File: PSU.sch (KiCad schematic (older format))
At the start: 11 parts

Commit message: Component placement
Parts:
- added J9: Conn_01x02, Connector_PinHeader_2.54mm:PinHeader_1x02_P2.54mm_Vertical, symbol Connector_Generic:Conn_01x02
- C1, C2: renamed from C?; footprint (none) -> Capacitor_SMD:C_0402_1005Metric
- D1, D2: renamed from D?; footprint (none) -> LED_SMD:LED_0603_1608Metric
- R3, R4, R5: renamed from R?; footprint (none) -> Resistor_SMD:R_0402_1005Metric
- gave numbers to parts that had none: 4
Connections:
- net GND: now also J9.2 (Pin_2)
- net VEXT: now also J9.1 (Pin_1)
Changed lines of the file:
@@
 $Descr A4 11693 8268
 encoding utf-8
-Sheet 2 5
+Sheet 2 4
 Title ""
 Date ""
@@
 P 7400 2200
 AR Path="/61CE9B73" Ref="U?"  Part="1"
-AR Path="/61CDC1C0/61CE9B73" Ref="U?"  Part="1"
-F 0 "U?" H 7400 2442 50  0000 C CNN
+AR Path="/61CDC1C0/61CE9B73" Ref="U1"  Part="1"
+F 0 "U1" H 7400 2442 50  0000 C CNN
 F 1 "AMS1117-3.3" H 7400 2351 50  0000 C CNN
 F 2 "Package_TO_SOT_SMD:SOT-223-3_TabPin2" H 7400 2400 50  0001 C CNN
@@
 P 7900 2400
 AR Path="/61CE9B79" Ref="C?"  Part="1"
-AR Path="/61CDC1C0/61CE9B79" Ref="C?"  Part="1"
-F 0 "C?" H 7988 2446 50  0000 L CNN
+AR Path="/61CDC1C0/61CE9B79" Ref="C2"  Part="1"
+F 0 "C2" H 7988 2446 50  0000 L CNN
 F 1 "22uF" H 7988 2355 50  0000 L CNN
-F 2 "" H 7900 2400 50  0001 C CNN
+F 2 "Capacitor_SMD:C_0402_1005Metric" H 7900 2400 50  0001 C CNN
 F 3 "~" H 7900 2400 50  0001 C CNN
 	1    7900 2400
@@
 P 6850 2400
 AR Path="/61CE9B7F" Ref="C?"  Part="1"
-AR Path="/61CDC1C0/61CE9B7F" Ref="C?"  Part="1"
-F 0 "C?" H 6938 2446 50  0000 L CNN
+AR Path="/61CDC1C0/61CE9B7F" Ref="C1"  Part="1"
+F 0 "C1" H 6938 2446 50  0000 L CNN
 F 1 "47uF" H 6938 2355 50  0000 L CNN
-F 2 "" H 6850 2400 50  0001 C CNN
+F 2 "Capacitor_SMD:C_0402_1005Metric" H 6850 2400 50  0001 C CNN
 F 3 "~" H 6850 2400 50  0001 C CNN
 	1    6850 2400
@@
 P 6850 2650
 AR Path="/61CE9B8F" Ref="#PWR?"  Part="1"
-AR Path="/61CDC1C0/61CE9B8F" Ref="#PWR?"  Part="1"
-F 0 "#PWR?" H 6850 2400 50  0001 C CNN
+AR Path="/61CDC1C0/61CE9B8F" Ref="#PWR022"  Part="1"
+F 0 "#PWR022" H 6850 2400 50  0001 C CNN
 F 1 "GND" H 6855 2477 50  0001 C CNN
 F 2 "" H 6850 2650 50  0001 C CNN
@@
 P 7900 2150
 AR Path="/61CE9B97" Ref="#PWR?"  Part="1"
-AR Path="/61CDC1C0/61CE9B97" Ref="#PWR?"  Part="1"
-F 0 "#PWR?" H 7900 2000 50  0001 C CNN
+AR Path="/61CDC1C0/61CE9B97" Ref="#PWR023"  Part="1"
+F 0 "#PWR023" H 7900 2000 50  0001 C CNN
 F 1 "+3V3" H 7915 2323 50  0000 C CNN
 F 2 "" H 7900 2150 50  0001 C CNN
@@
 P 6850 2150
 AR Path="/61CE9B9F" Ref="#PWR?"  Part="1"
-AR Path="/61CDC1C0/61CE9B9F" Ref="#PWR?"  Part="1"
-F 0 "#PWR?" H 6850 2000 50  0001 C CNN
+AR Path="/61CDC1C0/61CE9B9F" Ref="#PWR021"  Part="1"
+F 0 "#PWR021" H 6850 2000 50  0001 C CNN
 F 1 "+5V" H 6865 2323 50  0000 C CNN
 F 2 "" H 6850 2150 50  0001 C CNN
@@
 P 5000 3200
 AR Path="/61CE9BC3" Ref="#PWR?"  Part="1"
-AR Path="/61CDC1C0/61CE9BC3" Ref="#PWR?"  Part="1"
-F 0 "#PWR?" H 5000 2950 50  0001 C CNN
+AR Path="/61CDC1C0/61CE9BC3" Ref="#PWR019"  Part="1"
+F 0 "#PWR019" H 5000 2950 50  0001 C CNN
 F 1 "GND" H 5005 3027 50  0001 C CNN
 F 2 "" H 5000 3200 50  0001 C CNN
@@
 P 5000 2400
 AR Path="/61CE9BCE" Ref="R?"  Part="1"
-AR Path="/61CDC1C0/61CE9BCE" Ref="R?"  Part="1"
-F 0 "R?" H 5059 2446 50  0000 L CNN
+AR Path="/61CDC1C0/61CE9BCE" Ref="R4"  Part="1"
+F 0 "R4" H 5059 2446 50  0000 L CNN
 F 1 "47k" H 5059 2355 50  0000 L CNN
-F 2 "" H 5000 2400 50  0001 C CNN
+F 2 "Resistor_SMD:R_0402_1005Metric" H 5000 2400 50  0001 C CNN
 F 3 "~" H 5000 2400 50  0001 C CNN
 	1    5000 2400
@@
 P 4900 2950
 AR Path="/61CE9BD4" Ref="Q?"  Part="1"
-AR Path="/61CDC1C0/61CE9BD4" Ref="Q?"  Part="1"
-F 0 "Q?" H 5105 2996 50  0000 L CNN
+AR Path="/61CDC1C0/61CE9BD4" Ref="Q2"  Part="1"
+F 0 "Q2" H 5105 2996 50  0000 L CNN
 F 1 "AO3400A" H 5105 2905 50  0000 L CNN
 F 2 "Package_TO_SOT_SMD:SOT-23" H 5100 2875 50  0001 L CIN
@@
 P 4650 2300
 AR Path="/61CE9BDB" Ref="Q?"  Part="1"
-AR Path="/61CDC1C0/61CE9BDB" Ref="Q?"  Part="1"
-F 0 "Q?" V 4992 2300 50  0000 C CNN
+AR Path="/61CDC1C0/61CE9BDB" Ref="Q1"  Part="1"
+F 0 "Q1" V 4992 2300 50  0000 C CNN
 F 1 "AO3401A" V 4901 2300 50  0000 C CNN
 F 2 "Package_TO_SOT_SMD:SOT-23" H 4850 2225 50  0001 L CIN
@@
 P 5350 2300
 AR Path="/61CE9BE1" Ref="Q?"  Part="1"
-AR Path="/61CDC1C0/61CE9BE1" Ref="Q?"  Part="1"
-F 0 "Q?" V 5692 2300 50  0000 C CNN
+AR Path="/61CDC1C0/61CE9BE1" Ref="Q3"  Part="1"
+F 0 "Q3" V 5692 2300 50  0000 C CNN
 F 1 "AO3401A" V 5601 2300 50  0000 C CNN
 F 2 "Package_TO_SOT_SMD:SOT-23" H 5550 2225 50  0001 L CIN
@@
 P 5000 2100
 AR Path="/61CE9BE9" Ref="#PWR?"  Part="1"
-AR Path="/61CDC1C0/61CE9BE9" Ref="#PWR?"  Part="1"
-F 0 "#PWR?" H 5000 1950 50  0001 C CNN
+AR Path="/61CDC1C0/61CE9BE9" Ref="#PWR018"  Part="1"
+F 0 "#PWR018" H 5000 1950 50  0001 C CNN
 F 1 "+5V" H 5015 2273 50  0000 C CNN
 F 2 "" H 5000 2100 50  0001 C CNN
@@
 P 5650 2700
 AR Path="/61CE9BF0" Ref="D?"  Part="1"
-AR Path="/61CDC1C0/61CE9BF0" Ref="D?"  Part="1"
-F 0 "D?" V 5696 2630 50  0000 R CNN
+AR Path="/61CDC1C0/61CE9BF0" Ref="D2"  Part="1"
+F 0 "D2" V 5696 2630 50  0000 R CNN
 F 1 "YE" V 5605 2630 50  0000 R CNN
-F 2 "" V 5650 2700 50  0001 C CNN
+F 2 "LED_SMD:LED_0603_1608Metric" V 5650 2700 50  0001 C CNN
 F 3 "~" V 5650 2700 50  0001 C CNN
 	1    5650 2700
@@
 P 5650 2400
 AR Path="/61CE9BF6" Ref="R?"  Part="1"
-AR Path="/61CDC1C0/61CE9BF6" Ref="R?"  Part="1"
-F 0 "R?" H 5591 2446 50  0000 R CNN
+AR Path="/61CDC1C0/61CE9BF6" Ref="R5"  Part="1"
+F 0 "R5" H 5591 2446 50  0000 R CNN
 F 1 "220" H 5591 2355 50  0000 R CNN
-F 2 "" H 5650 2400 50  0001 C CNN
+F 2 "Resistor_SMD:R_0402_1005Metric" H 5650 2400 50  0001 C CNN
 F 3 "~" H 5650 2400 50  0001 C CNN
 	1    5650 2400
@@
 P 5650 2900
 AR Path="/61CE9C00" Ref="#PWR?"  Part="1"
-AR Path="/61CDC1C0/61CE9C00" Ref="#PWR?"  Part="1"
-F 0 "#PWR?" H 5650 2650 50  0001 C CNN
+AR Path="/61CDC1C0/61CE9C00" Ref="#PWR020"  Part="1"
+F 0 "#PWR020" H 5650 2650 50  0001 C CNN
 F 1 "GND" H 5655 2727 50  0001 C CNN
 F 2 "" H 5650 2900 50  0001 C CNN
@@
 P 4100 2700
 AR Path="/61CE9C07" Ref="D?"  Part="1"
-AR Path="/61CDC1C0/61CE9C07" Ref="D?"  Part="1"
-F 0 "D?" V 4146 2630 50  0000 R CNN
+AR Path="/61CDC1C0/61CE9C07" Ref="D1"  Part="1"
+F 0 "D1" V 4146 2630 50  0000 R CNN
 F 1 "GR" V 4055 2630 50  0000 R CNN
-F 2 "" V 4100 2700 50  0001 C CNN
+F 2 "LED_SMD:LED_0603_1608Metric" V 4100 2700 50  0001 C CNN
 F 3 "~" V 4100 2700 50  0001 C CNN
 	1    4100 2700
@@
 P 4100 2400
 AR Path="/61CE9C0D" Ref="R?"  Part="1"
-AR Path="/61CDC1C0/61CE9C0D" Ref="R?"  Part="1"
-F 0 "R?" H 4041 2446 50  0000 R CNN
+AR Path="/61CDC1C0/61CE9C0D" Ref="R3"  Part="1"
+F 0 "R3" H 4041 2446 50  0000 R CNN
 F 1 "220" H 4041 2355 50  0000 R CNN
-F 2 "" H 4100 2400 50  0001 C CNN
+F 2 "Resistor_SMD:R_0402_1005Metric" H 4100 2400 50  0001 C CNN
 F 3 "~" H 4100 2400 50  0001 C CNN
 	1    4100 2400
@@
 P 4100 2900
 AR Path="/61CE9C14" Ref="#PWR?"  Part="1"
-AR Path="/61CDC1C0/61CE9C14" Ref="#PWR?"  Part="1"
-F 0 "#PWR?" H 4100 2650 50  0001 C CNN
+AR Path="/61CDC1C0/61CE9C14" Ref="#PWR017"  Part="1"
+F 0 "#PWR017" H 4100 2650 50  0001 C CNN
 F 1 "GND" H 4105 2727 50  0001 C CNN
 F 2 "" H 4100 2900 50  0001 C CNN
@@
 Wire Wire Line
 	4100 2200 4350 2200
-Wire Wire Line
-	4100 2200 3950 2200
 Connection ~ 4100 2200
-Text HLabel 3950 2200 0    50   Input ~ 0
+$Comp
+L Connector_Generic:Conn_01x02 J?
+U 1 1 5FF7D0A3
+P 3300 2200
+AR Path="/5FF7D0A3" Ref="J?"  Part="1"
+AR Path="/61CDC1C0/5FF7D0A3" Ref="J9"  Part="1"
+F 0 "J9" H 3218 2325 50  0000 C CNN
+F 1 "Conn_01x02" H 3218 2326 50  0001 C CNN
+F 2 "Connector_PinHeader_2.54mm:PinHeader_1x02_P2.54mm_Vertical" H 3300 2200 50  0001 C CNN
+F 3 "~" H 3300 2200 50  0001 C CNN
+	1    3300 2200
+	-1   0    0    -1
+$EndComp
+Wire Wire Line
+	3500 2300 3550 2300
+Wire Wire Line
+	3550 2300 3550 2350
+$Comp
+L power:GND #PWR?
+U 1 1 5FF7D0AB
+P 3550 2350
+AR Path="/5FF7D0AB" Ref="#PWR?"  Part="1"
+AR Path="/61CDC1C0/5FF7D0AB" Ref="#PWR016"  Part="1"
+F 0 "#PWR016" H 3550 2100 50  0001 C CNN
+F 1 "GND" H 3555 2177 50  0001 C CNN
+F 2 "" H 3550 2350 50  0001 C CNN
+F 3 "" H 3550 2350 50  0001 C CNN
+	1    3550 2350
+	1    0    0    -1
+$EndComp
+Wire Wire Line
+	3500 2200 4100 2200
+Text Label 3650 2200 0    50   ~ 0
 VEXT
-Text HLabel 5800 2200 2    50   Input ~ 0
+Text GLabel 5800 2200 2    50   Input ~ 0
 VUSB
 $EndSCHEMATC

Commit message: Routing
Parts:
- C1: footprint Capacitor_SMD:C_0402_1005Metric -> Capacitor_SMD:C_Elec_6.3x7.7
- C2: value 22uF -> 100uF; footprint Capacitor_SMD:C_0402_1005Metric -> Capacitor_Tantalum_SMD:CP_EIA-3528-15_AVX-H
- J9: footprint Connector_PinHeader_2.54mm:PinHeader_1x02_P2.54mm_Vertical -> ak:Molex_022112022
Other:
- moved on the sheet: D1, D2, J9
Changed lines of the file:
@@
 AR Path="/61CDC1C0/61CE9B79" Ref="C2"  Part="1"
 F 0 "C2" H 7988 2446 50  0000 L CNN
-F 1 "22uF" H 7988 2355 50  0000 L CNN
-F 2 "Capacitor_SMD:C_0402_1005Metric" H 7900 2400 50  0001 C CNN
+F 1 "100uF" H 7988 2355 50  0000 L CNN
+F 2 "Capacitor_Tantalum_SMD:CP_EIA-3528-15_AVX-H" H 7900 2400 50  0001 C CNN
 F 3 "~" H 7900 2400 50  0001 C CNN
 	1    7900 2400
@@
 F 0 "C1" H 6938 2446 50  0000 L CNN
 F 1 "47uF" H 6938 2355 50  0000 L CNN
-F 2 "Capacitor_SMD:C_0402_1005Metric" H 6850 2400 50  0001 C CNN
+F 2 "Capacitor_SMD:C_Elec_6.3x7.7" H 6850 2400 50  0001 C CNN
 F 3 "~" H 6850 2400 50  0001 C CNN
 	1    6850 2400
@@
 L Device:LED_Small D?
 U 1 1 61CE9BF0
-P 5650 2700
+P 5650 2650
 AR Path="/61CE9BF0" Ref="D?"  Part="1"
 AR Path="/61CDC1C0/61CE9BF0" Ref="D2"  Part="1"
-F 0 "D2" V 5696 2630 50  0000 R CNN
-F 1 "YE" V 5605 2630 50  0000 R CNN
-F 2 "LED_SMD:LED_0603_1608Metric" V 5650 2700 50  0001 C CNN
-F 3 "~" V 5650 2700 50  0001 C CNN
-	1    5650 2700
+F 0 "D2" V 5696 2580 50  0000 R CNN
+F 1 "YE" V 5605 2580 50  0000 R CNN
+F 2 "LED_SMD:LED_0603_1608Metric" V 5650 2650 50  0001 C CNN
+F 3 "~" V 5650 2650 50  0001 C CNN
+	1    5650 2650
 	0    -1   -1   0
 $EndComp
@@
 $EndComp
 Wire Wire Line
-	5650 2600 5650 2500
+	5650 2550 5650 2500
 Wire Wire Line
 	5650 2300 5650 2200
@@
 L power:GND #PWR?
 U 1 1 61CE9C00
-P 5650 2900
+P 5650 2800
 AR Path="/61CE9C00" Ref="#PWR?"  Part="1"
 AR Path="/61CDC1C0/61CE9C00" Ref="#PWR020"  Part="1"
-F 0 "#PWR020" H 5650 2650 50  0001 C CNN
-F 1 "GND" H 5655 2727 50  0001 C CNN
-F 2 "" H 5650 2900 50  0001 C CNN
-F 3 "" H 5650 2900 50  0001 C CNN
-	1    5650 2900
-	-1   0    0    -1
-$EndComp
-Wire Wire Line
-	5650 2900 5650 2800
+F 0 "#PWR020" H 5650 2550 50  0001 C CNN
+F 1 "GND" H 5655 2627 50  0001 C CNN
+F 2 "" H 5650 2800 50  0001 C CNN
+F 3 "" H 5650 2800 50  0001 C CNN
+	1    5650 2800
+	-1   0    0    -1
+$EndComp
+Wire Wire Line
+	5650 2800 5650 2750
 $Comp
 L Device:LED_Small D?
 U 1 1 61CE9C07
-P 4100 2700
+P 4100 2650
 AR Path="/61CE9C07" Ref="D?"  Part="1"
 AR Path="/61CDC1C0/61CE9C07" Ref="D1"  Part="1"
-F 0 "D1" V 4146 2630 50  0000 R CNN
-F 1 "GR" V 4055 2630 50  0000 R CNN
-F 2 "LED_SMD:LED_0603_1608Metric" V 4100 2700 50  0001 C CNN
-F 3 "~" V 4100 2700 50  0001 C CNN
-	1    4100 2700
+F 0 "D1" V 4146 2580 50  0000 R CNN
+F 1 "GR" V 4055 2580 50  0000 R CNN
+F 2 "LED_SMD:LED_0603_1608Metric" V 4100 2650 50  0001 C CNN
+F 3 "~" V 4100 2650 50  0001 C CNN
+	1    4100 2650
 	0    -1   -1   0
 $EndComp
@@
 $EndComp
 Wire Wire Line
-	4100 2600 4100 2500
+	4100 2550 4100 2500
 $Comp
 L power:GND #PWR?
 U 1 1 61CE9C14
-P 4100 2900
+P 4100 2800
 AR Path="/61CE9C14" Ref="#PWR?"  Part="1"
 AR Path="/61CDC1C0/61CE9C14" Ref="#PWR017"  Part="1"
-F 0 "#PWR017" H 4100 2650 50  0001 C CNN
-F 1 "GND" H 4105 2727 50  0001 C CNN
-F 2 "" H 4100 2900 50  0001 C CNN
-F 3 "" H 4100 2900 50  0001 C CNN
-	1    4100 2900
-	-1   0    0    -1
-$EndComp
-Wire Wire Line
-	4100 2900 4100 2800
+F 0 "#PWR017" H 4100 2550 50  0001 C CNN
+F 1 "GND" H 4105 2627 50  0001 C CNN
+F 2 "" H 4100 2800 50  0001 C CNN
+F 3 "" H 4100 2800 50  0001 C CNN
+	1    4100 2800
+	-1   0    0    -1
+$EndComp
+Wire Wire Line
+	4100 2800 4100 2750
 Wire Wire Line
 	4100 2300 4100 2200
-Wire Wire Line
-	4100 2200 4350 2200
 Connection ~ 4100 2200
 $Comp
 L Connector_Generic:Conn_01x02 J?
 U 1 1 5FF7D0A3
-P 3300 2200
+P 3400 2200
 AR Path="/5FF7D0A3" Ref="J?"  Part="1"
 AR Path="/61CDC1C0/5FF7D0A3" Ref="J9"  Part="1"
-F 0 "J9" H 3218 2325 50  0000 C CNN
-F 1 "Conn_01x02" H 3218 2326 50  0001 C CNN
-F 2 "Connector_PinHeader_2.54mm:PinHeader_1x02_P2.54mm_Vertical" H 3300 2200 50  0001 C CNN
-F 3 "~" H 3300 2200 50  0001 C CNN
-	1    3300 2200
-	-1   0    0    -1
-$EndComp
-Wire Wire Line
-	3500 2300 3550 2300
-Wire Wire Line
-	3550 2300 3550 2350
+F 0 "J9" H 3318 2325 50  0000 C CNN
+F 1 "Conn_01x02" H 3318 2326 50  0001 C CNN
+F 2 "ak:Molex_022112022" H 3400 2200 50  0001 C CNN
+F 3 "~" H 3400 2200 50  0001 C CNN
+	1    3400 2200
+	-1   0    0    -1
+$EndComp
+Wire Wire Line
+	3600 2300 3650 2300
+Wire Wire Line
+	3650 2300 3650 2350
 $Comp
 L power:GND #PWR?
 U 1 1 5FF7D0AB
-P 3550 2350
+P 3650 2350
 AR Path="/5FF7D0AB" Ref="#PWR?"  Part="1"
 AR Path="/61CDC1C0/5FF7D0AB" Ref="#PWR016"  Part="1"
-F 0 "#PWR016" H 3550 2100 50  0001 C CNN
-F 1 "GND" H 3555 2177 50  0001 C CNN
-F 2 "" H 3550 2350 50  0001 C CNN
-F 3 "" H 3550 2350 50  0001 C CNN
-	1    3550 2350
-	1    0    0    -1
-$EndComp
-Wire Wire Line
-	3500 2200 4100 2200
+F 0 "#PWR016" H 3650 2100 50  0001 C CNN
+F 1 "GND" H 3655 2177 50  0001 C CNN
+F 2 "" H 3650 2350 50  0001 C CNN
+F 3 "" H 3650 2350 50  0001 C CNN
+	1    3650 2350
+	1    0    0    -1
+$EndComp
+Wire Wire Line
+	3600 2200 4100 2200
 Text Label 3650 2200 0    50   ~ 0
 VEXT
 Text GLabel 5800 2200 2    50   Input ~ 0
 VUSB
+Wire Wire Line
+	4100 2200 4350 2200
 $EndSCHEMATC

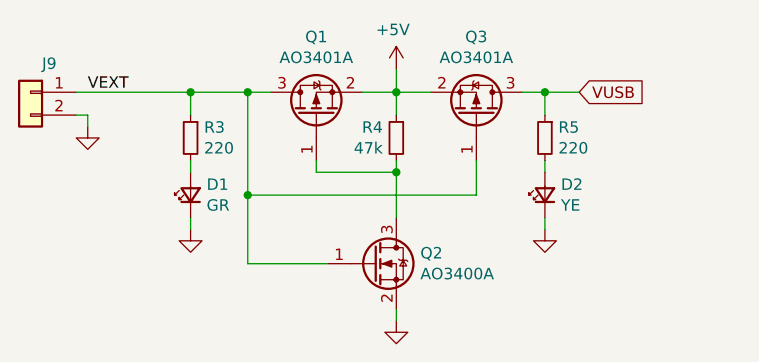
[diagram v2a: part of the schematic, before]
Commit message: Added ESD protection
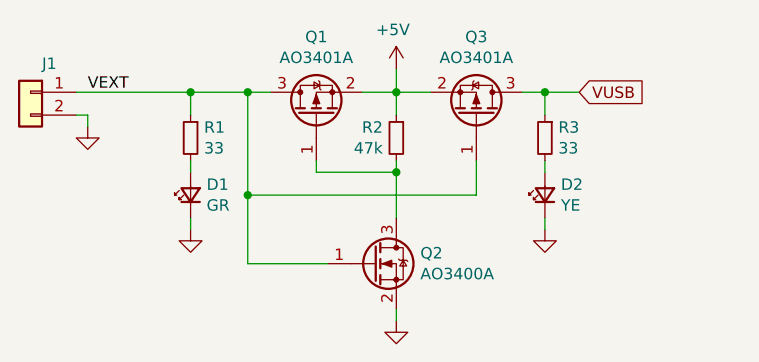
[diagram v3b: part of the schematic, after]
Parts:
- R1: renamed from R3; value 220 -> 33
- R3: renamed from R5; value 220 -> 33
- renumbered J9 to J1, R4 to R2
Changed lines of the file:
@@
 $Descr A4 11693 8268
 encoding utf-8
-Sheet 2 4
+Sheet 2 5
 Title ""
 Date ""
@@
 P 6850 2650
 AR Path="/61CE9B8F" Ref="#PWR?"  Part="1"
-AR Path="/61CDC1C0/61CE9B8F" Ref="#PWR022"  Part="1"
-F 0 "#PWR022" H 6850 2400 50  0001 C CNN
+AR Path="/61CDC1C0/61CE9B8F" Ref="#PWR011"  Part="1"
+F 0 "#PWR011" H 6850 2400 50  0001 C CNN
 F 1 "GND" H 6855 2477 50  0001 C CNN
 F 2 "" H 6850 2650 50  0001 C CNN
@@
 P 7900 2150
 AR Path="/61CE9B97" Ref="#PWR?"  Part="1"
-AR Path="/61CDC1C0/61CE9B97" Ref="#PWR023"  Part="1"
-F 0 "#PWR023" H 7900 2000 50  0001 C CNN
+AR Path="/61CDC1C0/61CE9B97" Ref="#PWR012"  Part="1"
+F 0 "#PWR012" H 7900 2000 50  0001 C CNN
 F 1 "+3V3" H 7915 2323 50  0000 C CNN
 F 2 "" H 7900 2150 50  0001 C CNN
@@
 P 6850 2150
 AR Path="/61CE9B9F" Ref="#PWR?"  Part="1"
-AR Path="/61CDC1C0/61CE9B9F" Ref="#PWR021"  Part="1"
-F 0 "#PWR021" H 6850 2000 50  0001 C CNN
+AR Path="/61CDC1C0/61CE9B9F" Ref="#PWR010"  Part="1"
+F 0 "#PWR010" H 6850 2000 50  0001 C CNN
 F 1 "+5V" H 6865 2323 50  0000 C CNN
 F 2 "" H 6850 2150 50  0001 C CNN
@@
 P 5000 3200
 AR Path="/61CE9BC3" Ref="#PWR?"  Part="1"
-AR Path="/61CDC1C0/61CE9BC3" Ref="#PWR019"  Part="1"
-F 0 "#PWR019" H 5000 2950 50  0001 C CNN
+AR Path="/61CDC1C0/61CE9BC3" Ref="#PWR08"  Part="1"
+F 0 "#PWR08" H 5000 2950 50  0001 C CNN
 F 1 "GND" H 5005 3027 50  0001 C CNN
 F 2 "" H 5000 3200 50  0001 C CNN
@@
 P 5000 2400
 AR Path="/61CE9BCE" Ref="R?"  Part="1"
-AR Path="/61CDC1C0/61CE9BCE" Ref="R4"  Part="1"
-F 0 "R4" H 5059 2446 50  0000 L CNN
+AR Path="/61CDC1C0/61CE9BCE" Ref="R2"  Part="1"
+F 0 "R2" H 5059 2446 50  0000 L CNN
 F 1 "47k" H 5059 2355 50  0000 L CNN
 F 2 "Resistor_SMD:R_0402_1005Metric" H 5000 2400 50  0001 C CNN
@@
 P 5000 2100
 AR Path="/61CE9BE9" Ref="#PWR?"  Part="1"
-AR Path="/61CDC1C0/61CE9BE9" Ref="#PWR018"  Part="1"
-F 0 "#PWR018" H 5000 1950 50  0001 C CNN
+AR Path="/61CDC1C0/61CE9BE9" Ref="#PWR07"  Part="1"
+F 0 "#PWR07" H 5000 1950 50  0001 C CNN
 F 1 "+5V" H 5015 2273 50  0000 C CNN
 F 2 "" H 5000 2100 50  0001 C CNN
@@
 P 5650 2400
 AR Path="/61CE9BF6" Ref="R?"  Part="1"
-AR Path="/61CDC1C0/61CE9BF6" Ref="R5"  Part="1"
-F 0 "R5" H 5591 2446 50  0000 R CNN
-F 1 "220" H 5591 2355 50  0000 R CNN
+AR Path="/61CDC1C0/61CE9BF6" Ref="R3"  Part="1"
+F 0 "R3" H 5591 2446 50  0000 R CNN
+F 1 "33" H 5591 2355 50  0000 R CNN
 F 2 "Resistor_SMD:R_0402_1005Metric" H 5650 2400 50  0001 C CNN
 F 3 "~" H 5650 2400 50  0001 C CNN
@@
 P 5650 2800
 AR Path="/61CE9C00" Ref="#PWR?"  Part="1"
-AR Path="/61CDC1C0/61CE9C00" Ref="#PWR020"  Part="1"
-F 0 "#PWR020" H 5650 2550 50  0001 C CNN
+AR Path="/61CDC1C0/61CE9C00" Ref="#PWR09"  Part="1"
+F 0 "#PWR09" H 5650 2550 50  0001 C CNN
 F 1 "GND" H 5655 2627 50  0001 C CNN
 F 2 "" H 5650 2800 50  0001 C CNN
@@
 P 4100 2400
 AR Path="/61CE9C0D" Ref="R?"  Part="1"
-AR Path="/61CDC1C0/61CE9C0D" Ref="R3"  Part="1"
-F 0 "R3" H 4041 2446 50  0000 R CNN
-F 1 "220" H 4041 2355 50  0000 R CNN
+AR Path="/61CDC1C0/61CE9C0D" Ref="R1"  Part="1"
+F 0 "R1" H 4041 2446 50  0000 R CNN
+F 1 "33" H 4041 2355 50  0000 R CNN
 F 2 "Resistor_SMD:R_0402_1005Metric" H 4100 2400 50  0001 C CNN
 F 3 "~" H 4100 2400 50  0001 C CNN
@@
 P 4100 2800
 AR Path="/61CE9C14" Ref="#PWR?"  Part="1"
-AR Path="/61CDC1C0/61CE9C14" Ref="#PWR017"  Part="1"
-F 0 "#PWR017" H 4100 2550 50  0001 C CNN
+AR Path="/61CDC1C0/61CE9C14" Ref="#PWR06"  Part="1"
+F 0 "#PWR06" H 4100 2550 50  0001 C CNN
 F 1 "GND" H 4105 2627 50  0001 C CNN
 F 2 "" H 4100 2800 50  0001 C CNN
@@
 P 3400 2200
 AR Path="/5FF7D0A3" Ref="J?"  Part="1"
-AR Path="/61CDC1C0/5FF7D0A3" Ref="J9"  Part="1"
-F 0 "J9" H 3318 2325 50  0000 C CNN
+AR Path="/61CDC1C0/5FF7D0A3" Ref="J1"  Part="1"
+F 0 "J1" H 3318 2325 50  0000 C CNN
 F 1 "Conn_01x02" H 3318 2326 50  0001 C CNN
 F 2 "ak:Molex_022112022" H 3400 2200 50  0001 C CNN
@@
 P 3650 2350
 AR Path="/5FF7D0AB" Ref="#PWR?"  Part="1"
-AR Path="/61CDC1C0/5FF7D0AB" Ref="#PWR016"  Part="1"
-F 0 "#PWR016" H 3650 2100 50  0001 C CNN
+AR Path="/61CDC1C0/5FF7D0AB" Ref="#PWR05"  Part="1"
+F 0 "#PWR05" H 3650 2100 50  0001 C CNN
 F 1 "GND" H 3655 2177 50  0001 C CNN
 F 2 "" H 3650 2350 50  0001 C CNN
